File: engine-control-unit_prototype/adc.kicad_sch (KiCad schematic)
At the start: 36 parts, among them J18 VREF, J19 PT1, J20 PT2, J21 PT3, J22 PT4, J23 PT5, U11 INA826, U12 ADS131M04xPW

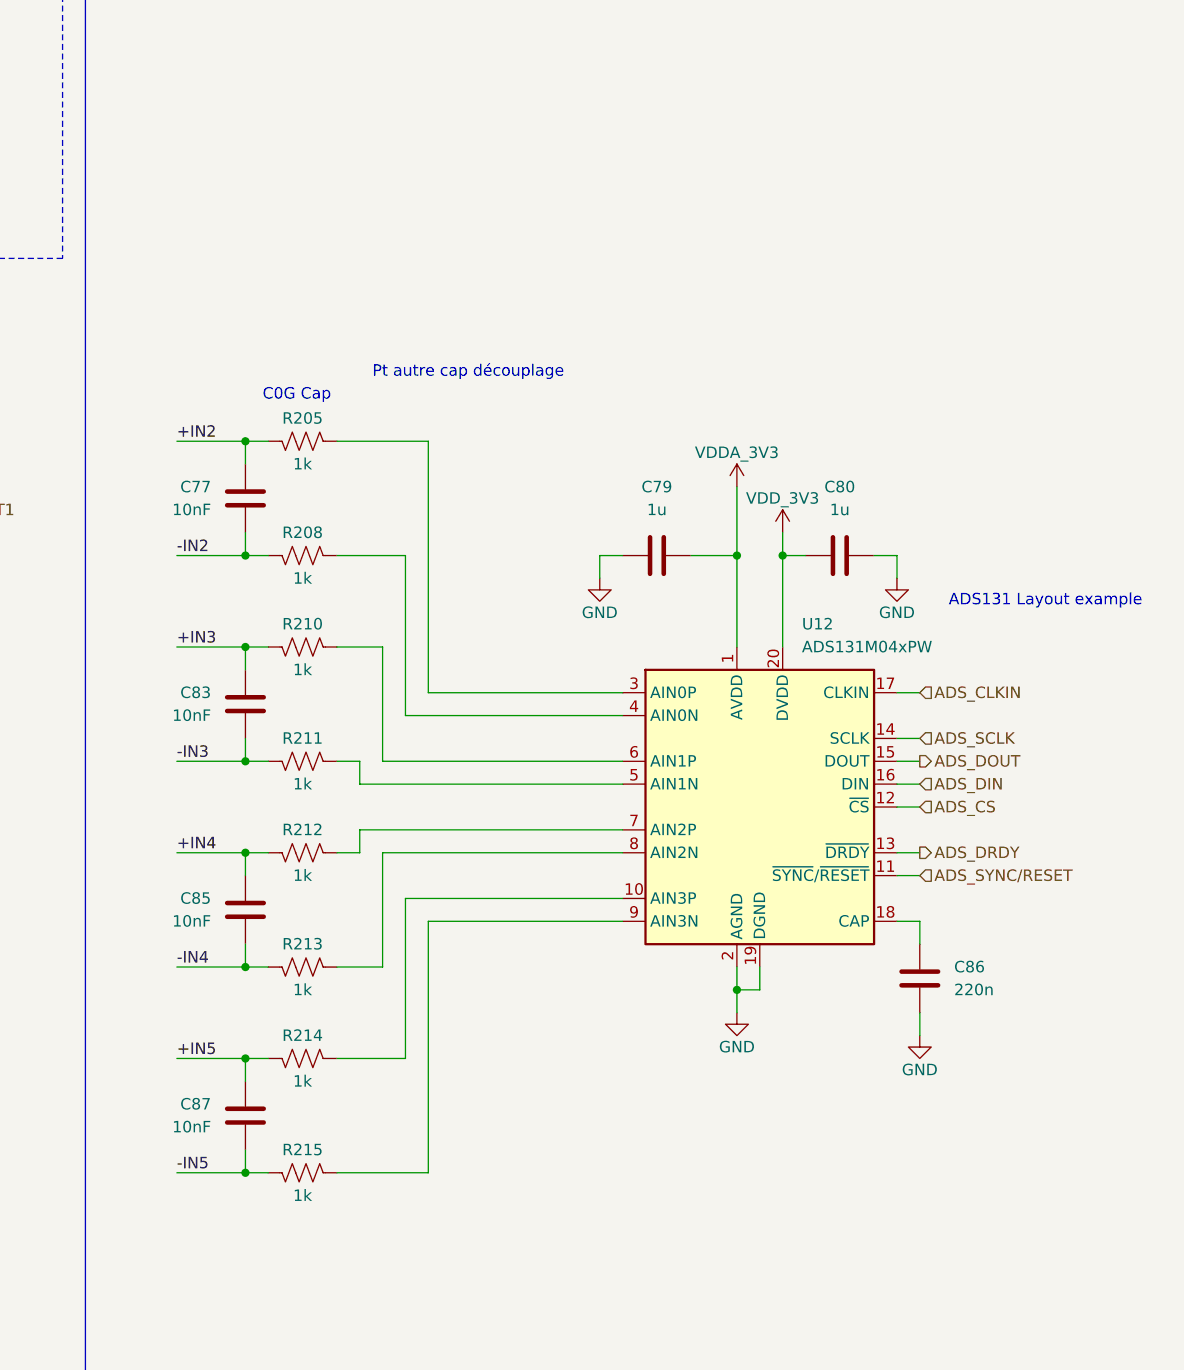
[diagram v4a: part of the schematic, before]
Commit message: VDD_3V3 is now VDD_3V6 (Removed LDO) LEDs now have the right symbol (oops x2)
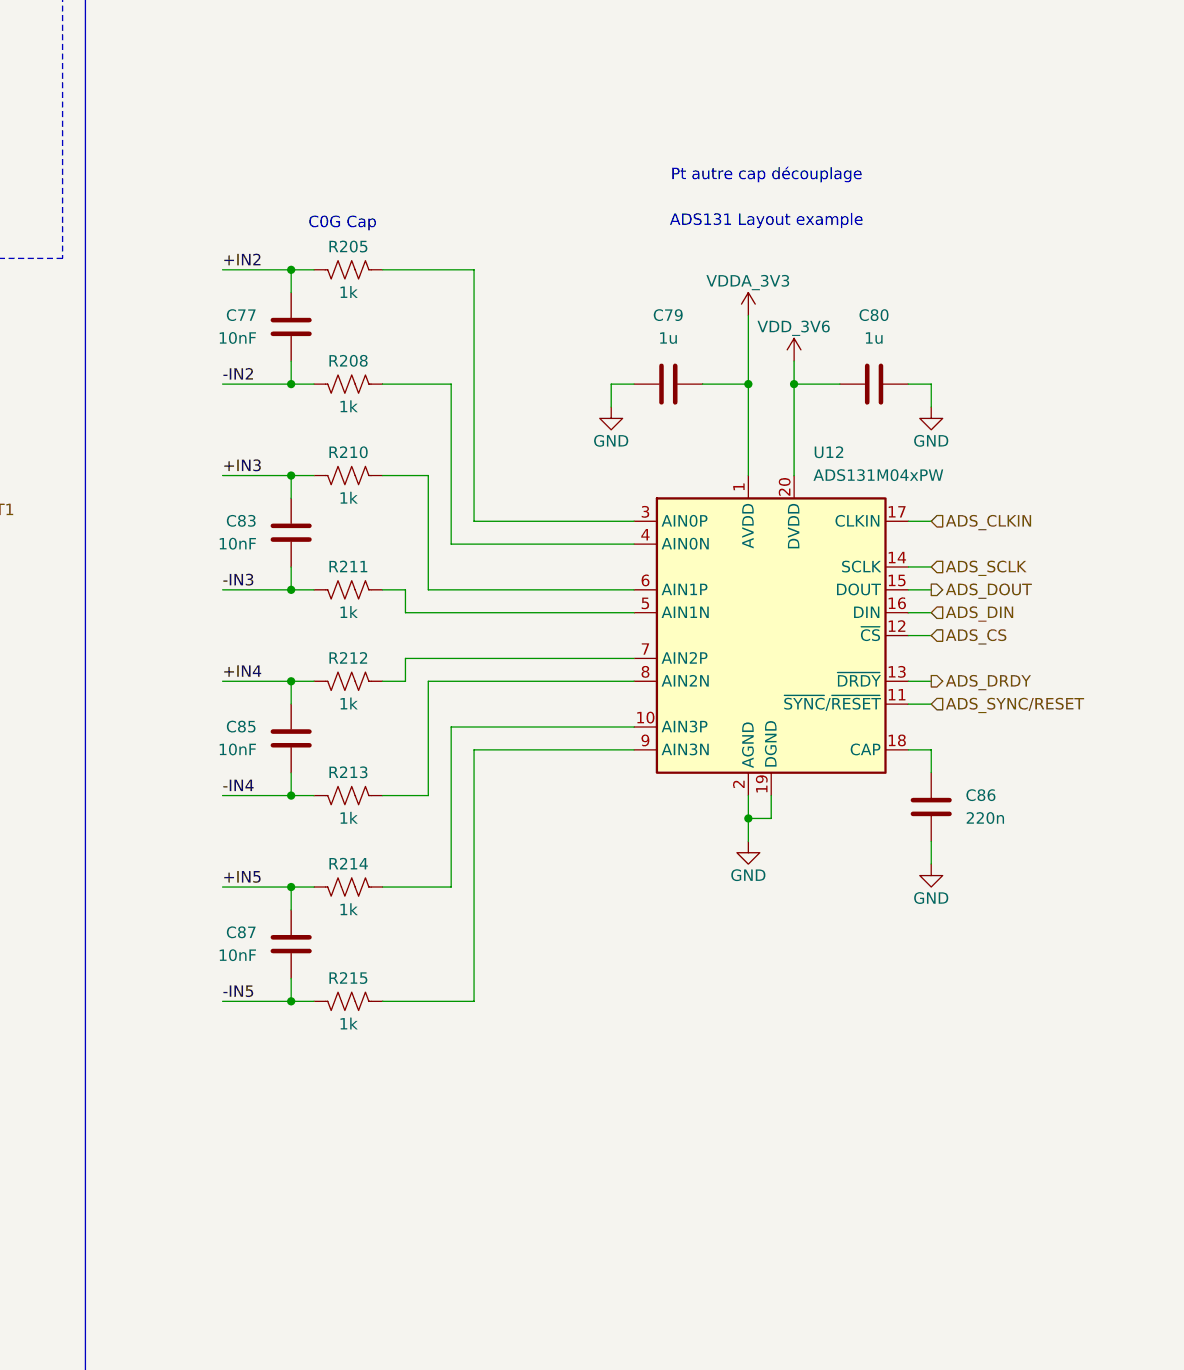
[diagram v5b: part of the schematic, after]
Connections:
- net VDD_3V3 renamed VDD_3V6
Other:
- moved on the sheet: C77, C79, C80, C83, C85, C86, C87, R205, R208, R210, R211, R212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

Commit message: Started layout Added some footprints
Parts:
- removed JP3: PIN/GND, symbol Jumper:Jumper_3_Bridged12
- removed TP1: PT1, symbol Connector:TestPoint
- added JP3: PIN / GND, Jumper:SolderJumper-3_P1.3mm_Bridged12_RoundedPad1.0x1.5mm, symbol Jumper:SolderJumper_3_Bridged12
- C75: value 0.1u -> 0u1; footprint Capacitor_SMD:C_0603_1608Metric -> Capacitor_SMD:C_0402_1005Metric
- C76, C78, C79, C80, C82: footprint Capacitor_SMD:C_0603_1608Metric -> Capacitor_SMD:C_0402_1005Metric
- C77, C83, C85, C87: value 10nF -> 10n
- C81: now not fitted
- J18: footprint (none) -> Connector_PinHeader_2.54mm:PinHeader_1x01_P2.54mm_Vertical
- J19, J20, J21, J22, J23: footprint (none) -> Connector_PinSocket_2.54mm:PinSocket_1x04_P2.54mm_Vertical
- JP2: footprint (none) -> Jumper:SolderJumper-3_P1.3mm_Open_RoundedPad1.0x1.5mm
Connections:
- net GND: now also JP3.1 (A)
- net at J18.1 (Pin_1): now also JP3.3 (B)
- net at U11.6 (REF): now also JP3.2 (C)
- net VDD_3V6 renamed VDD_3V3
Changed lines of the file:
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@@
 	)
 	(junction
-		(at 132.08 83.82)
-		(diameter 0)
-		(color 0 0 0 0)
-	)
-	(junction
 		(at 190.5 115.57)
 		(diameter 0)
@@
 	(wire
 		(pts
-			(xy 132.08 81.28) (xy 132.08 83.82)
-		)
-		(stroke
-			(width 0)
-			(type default)
-		)
-	)
-	(wire
-		(pts
 			(xy 73.66 76.2) (xy 97.79 76.2)
 		)
@@
 	(wire
 		(pts
-			(xy 125.73 63.5) (xy 128.27 63.5)
+			(xy 125.73 63.5) (xy 129.54 63.5)
 		)
 		(stroke
@@
 	(wire
 		(pts
-			(xy 125.73 83.82) (xy 132.08 83.82)
+			(xy 125.73 83.82) (xy 137.16 83.82)
 		)
 		(stroke
@@
 	(wire
 		(pts
-			(xy 205.74 102.87) (xy 205.74 115.57)
+			(xy 139.7 63.5) (xy 143.51 63.5)
 		)
 		(stroke
@@
 	(wire
 		(pts
-			(xy 143.51 63.5) (xy 140.97 63.5)
+			(xy 205.74 102.87) (xy 205.74 115.57)
 		)
 		(stroke
@@
 	(wire
 		(pts
-			(xy 132.08 83.82) (xy 137.16 83.82)
-		)
-		(stroke
-			(width 0)
-			(type default)
-		)
-	)
-	(wire
-		(pts
 			(xy 33.02 52.07) (xy 33.02 54.61)
 		)
@@
 			)
 		)
-		(property "Footprint" "Capacitor_SMD:C_0603_1608Metric"
+		(property "Footprint" "Capacitor_SMD:C_0402_1005Metric"
 			(at 72.6948 93.98 0)
 			(effects
@@
 			)
 		)
-		(property "Footprint" ""
+		(property "Footprint" "Connector_PinHeader_2.54mm:PinHeader_1x01_P2.54mm_Vertical"
 			(at 120.65 63.5 0)
 			(effects
@@
 			)
 		)
-		(property "Footprint" ""
+		(property "Footprint" "Jumper:SolderJumper-3_P1.3mm_Open_RoundedPad1.0x1.5mm"
 			(at 33.02 58.42 0)
 			(effects
@@
 		(in_bom yes)
 		(on_board yes)
-		(dnp no)
+		(dnp yes)
 		(property "Reference" "C81"
 			(at 152.4 88.9 0)
@@
 			)
 		)
-		(property "Value" "10nF"
+		(property "Value" "10n"
 			(at 186.69 64.7699 0)
 			(effects
@@
 			)
 		)
-		(property "Footprint" "Capacitor_SMD:C_0603_1608Metric"
+		(property "Footprint" "Capacitor_SMD:C_0402_1005Metric"
 			(at 72.6948 80.01 0)
 			(effects
@@
 			)
 		)
-		(property "Footprint" "Capacitor_SMD:C_0603_1608Metric"
+		(property "Footprint" "Capacitor_SMD:C_0402_1005Metric"
 			(at 236.22 70.8152 0)
 			(effects
@@
 			)
 		)
-		(property "Footprint" ""
+		(property "Footprint" "Connector_PinSocket_2.54mm:PinSocket_1x04_P2.54mm_Vertical"
 			(at 31.75 139.7 0)
 			(effects
@@
 	)
 	(symbol
-		(lib_id "Connector:TestPoint")
-		(at 132.08 81.28 0)
-		(unit 1)
-		(exclude_from_sim no)
-		(in_bom yes)
-		(on_board yes)
-		(dnp no)
-		(fields_autoplaced yes)
-		(property "Reference" "TP1"
-			(at 134.62 76.7079 0)
-			(effects
-				(font
-					(size 1.27 1.27)
-				)
-				(justify left)
-			)
-		)
-		(property "Value" "PT1"
-			(at 134.62 79.2479 0)
-			(effects
-				(font
-					(size 1.27 1.27)
-				)
-				(justify left)
-			)
-		)
-		(property "Footprint" ""
-			(at 137.16 81.28 0)
-			(effects
-				(font
-					(size 1.27 1.27)
-				)
-				(hide yes)
-			)
-		)
-		(property "Datasheet" "~"
-			(at 137.16 81.28 0)
-			(effects
-				(font
-					(size 1.27 1.27)
-				)
-				(hide yes)
-			)
-		)
-		(property "Description" "test point"
-			(at 132.08 81.28 0)
-			(effects
-				(font
-					(size 1.27 1.27)
-				)
-				(hide yes)
-			)
-		)
-		(pin "1"
-		)
-		(instances
-			(project "engine-control-unit_prototype"
-				(path "/4da294f1-7505-49eb-91fe-5b5cfad6e8fb/934d114b-d4b5-4669-b5e9-a82bebed1d7a"
-					(reference "TP1")
-					(unit 1)
-				)
-			)
-		)
-	)
-	(symbol
 		(lib_id "power:GND")
 		(at 241.3 120.65 0)
@@
 			)
 		)
-		(property "Value" "10nF"
+		(property "Value" "10n"
 			(at 186.69 87.6299 0)
 			(effects
@@
 	)
 	(symbol
-		(lib_id "Jumper:Jumper_3_Bridged12")
-		(at 134.62 63.5 0)
-		(mirror y)
-		(unit 1)
-		(exclude_from_sim no)
-		(in_bom no)
-		(on_board yes)
-		(dnp no)
-		(fields_autoplaced yes)
-		(property "Reference" "JP3"
-			(at 134.62 59.69 0)
-			(effects
-				(font
-					(size 1.27 1.27)
-				)
-			)
-		)
-		(property "Value" "PIN/GND"
-			(at 134.62 57.15 0)
-			(effects
-				(font
-					(size 1.27 1.27)
-				)
-			)
-		)
-		(property "Footprint" ""
-			(at 134.62 63.5 0)
-			(effects
-				(font
-					(size 1.27 1.27)
-				)
-				(hide yes)
-			)
-		)
-		(property "Datasheet" "~"
-			(at 134.62 63.5 0)
-			(effects
-				(font
-					(size 1.27 1.27)
-				)
-				(hide yes)
-			)
-		)
-		(property "Description" "Jumper, 3-pole, pins 1+2 closed/bridged"
-			(at 134.62 63.5 0)
-			(effects
-				(font
-					(size 1.27 1.27)
-				)
-				(hide yes)
-			)
-		)
-		(pin "2"
-		)
-		(pin "1"
-		)
-		(pin "3"
-		)
-		(instances
-			(project "engine-control-unit_prototype"
-				(path "/4da294f1-7505-49eb-91fe-5b5cfad6e8fb/934d114b-d4b5-4669-b5e9-a82bebed1d7a"
-					(reference "JP3")
-					(unit 1)
-				)
-			)
-		)
-	)
-	(symbol
 		(lib_id "power:VDD")
 		(at 25.4 101.6 0)
@@
 			)
 		)
-		(property "Footprint" ""
+		(property "Footprint" "Connector_PinSocket_2.54mm:PinSocket_1x04_P2.54mm_Vertical"
 			(at 31.75 82.55 0)
 			(effects
@@
 			)
 		)
-		(property "Value" "10nF"
+		(property "Value" "10n"
 			(at 186.69 110.4899 0)
 			(effects
@@
 			)
 		)
-		(property "Footprint" ""
+		(property "Footprint" "Connector_PinSocket_2.54mm:PinSocket_1x04_P2.54mm_Vertical"
 			(at 73.66 139.7 0)
 			(effects
@@
 			)
 		)
-		(property "Footprint" "Capacitor_SMD:C_0603_1608Metric"
+		(property "Footprint" "Capacitor_SMD:C_0402_1005Metric"
 			(at 72.6948 64.77 0)
 			(effects
@@
 			)
 		)
-		(property "Footprint" ""
+		(property "Footprint" "Connector_PinSocket_2.54mm:PinSocket_1x04_P2.54mm_Vertical"
 			(at 52.07 139.7 0)
 			(effects
@@
 			)
 		)
-		(property "Value" "10nF"
+		(property "Value" "10n"
 			(at 186.69 133.3499 0)
 			(effects
@@
 			)
 		)
-		(property "Value" "0.1u"
+		(property "Value" "0u1"
 			(at 106.68 60.96 90)
 			(effects
@@
 			)
 		)
-		(property "Footprint" "Capacitor_SMD:C_0603_1608Metric"
+		(property "Footprint" "Capacitor_SMD:C_0402_1005Metric"
 			(at 110.49 67.0052 0)
 			(effects
@@
 	)
 	(symbol
+		(lib_id "Jumper:SolderJumper_3_Bridged12")
+		(at 134.62 63.5 0)
+		(mirror y)
+		(unit 1)
+		(exclude_from_sim no)
+		(in_bom no)
+		(on_board yes)
+		(dnp no)
+		(property "Reference" "JP3"
+			(at 130.556 67.056 0)
+			(effects
+				(font
+					(size 1.27 1.27)
+				)
+			)
+		)
+		(property "Value" "PIN / GND"
+			(at 134.62 60.706 0)
+			(effects
+				(font
+					(size 1.27 1.27)
+				)
+			)
+		)
+		(property "Footprint" "Jumper:SolderJumper-3_P1.3mm_Bridged12_RoundedPad1.0x1.5mm"
+			(at 134.62 63.5 0)
+			(effects
+				(font
+					(size 1.27 1.27)
+				)
+				(hide yes)
+			)
+		)
+		(property "Datasheet" "~"
+			(at 134.62 63.5 0)
+			(effects
+				(font
+					(size 1.27 1.27)
+				)
+				(hide yes)
+			)
+		)
+		(property "Description" "3-pole Solder Jumper, pins 1+2 closed/bridged"
+			(at 134.62 63.5 0)
+			(effects
+				(font
+					(size 1.27 1.27)
+				)
+				(hide yes)
+			)
+		)
+		(pin "3"
+		)
+		(pin "2"
+		)
+		(pin "1"
+		)
+		(instances
+			(project "engine-control-unit_prototype"
+				(path "/4da294f1-7505-49eb-91fe-5b5cfad6e8fb/934d114b-d4b5-4669-b5e9-a82bebed1d7a"
+					(reference "JP3")
+					(unit 1)
+				)
+			)
+		)
+	)
+	(symbol
 		(lib_id "Connector:Screw_Terminal_01x04")
 		(at 95.25 139.7 0)
@@
 			)
 		)
-		(property "Footprint" ""
+		(property "Footprint" "Connector_PinSocket_2.54mm:PinSocket_1x04_P2.54mm_Vertical"
 			(at 95.25 139.7 0)
 			(effects
@@
 			)
 		)
-		(property "Value" "VDD_3V6"
+		(property "Value" "VDD_3V3"
 			(at 246.38 63.5 0)
 			(effects
@@
 			)
 		)
-		(property "Footprint" "Capacitor_SMD:C_0603_1608Metric"
+		(property "Footprint" "Capacitor_SMD:C_0402_1005Metric"
 			(at 259.08 70.8152 0)
 			(effects
